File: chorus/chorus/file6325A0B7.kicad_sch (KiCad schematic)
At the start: 18 parts

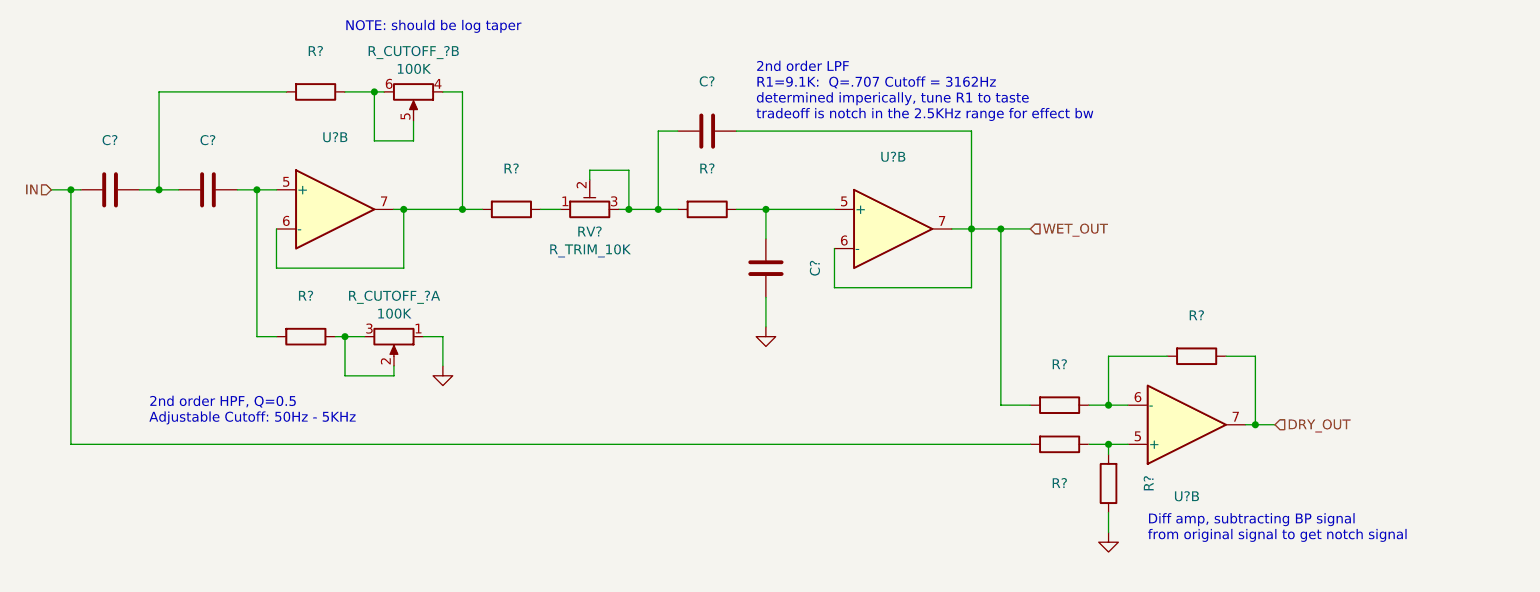
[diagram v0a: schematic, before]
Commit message: add output buffer
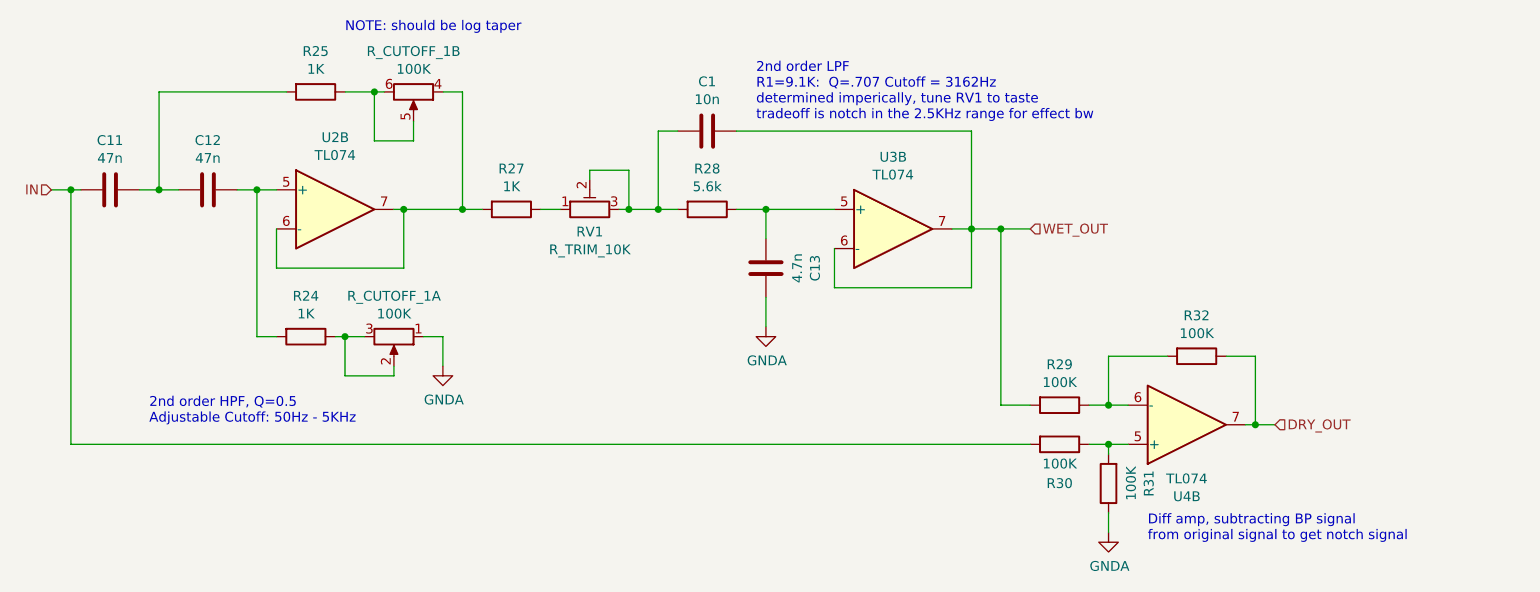
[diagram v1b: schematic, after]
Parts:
- C1: renamed from C?; value (none) -> 10n
- C11, C12: renamed from C?; value (none) -> 47n
- C13: renamed from C?; value (none) -> 4.7n
- R24, R25, R27: renamed from R?; value (none) -> 1K
- R28: renamed from R?; value (none) -> 5.6k
- R29, R30, R31, R32: renamed from R?; value (none) -> 100K
- U2, U3, U4: renamed from U?; value (none) -> TL074
- gave numbers to parts that had none: 2
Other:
- note added: "2nd order LPF R1=9.1K: Q=.707 Cutoff = 3162Hz determined imperically, tune RV1 to taste tradeoff is notch in the 2.5KHz range for effect bw"
- note removed: "2nd order LPF R1=9.1K: Q=.707 Cutoff = 3162Hz determined imperically, tune R1 to taste tradeoff is notch in the 2.5KHz range for effect bw"
- company: (none) -> rabidaudio
